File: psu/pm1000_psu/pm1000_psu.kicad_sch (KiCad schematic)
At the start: 48 parts, among them J1 Screw_Terminal_01x04, J10 Conn_01x03_Male, J2 Conn_01x03_Male, J3 Phantom A switch, J4 Phantom A Led, J5 Conn_01x02_Male, J6 Conn_01x03_Male, J7 Phantom B switch, J8 Phantom B Led, J9 Conn_01x03_Male, U1 LM317_TO-220, U2 LM317_TO-220, U3 LM317_TO-220

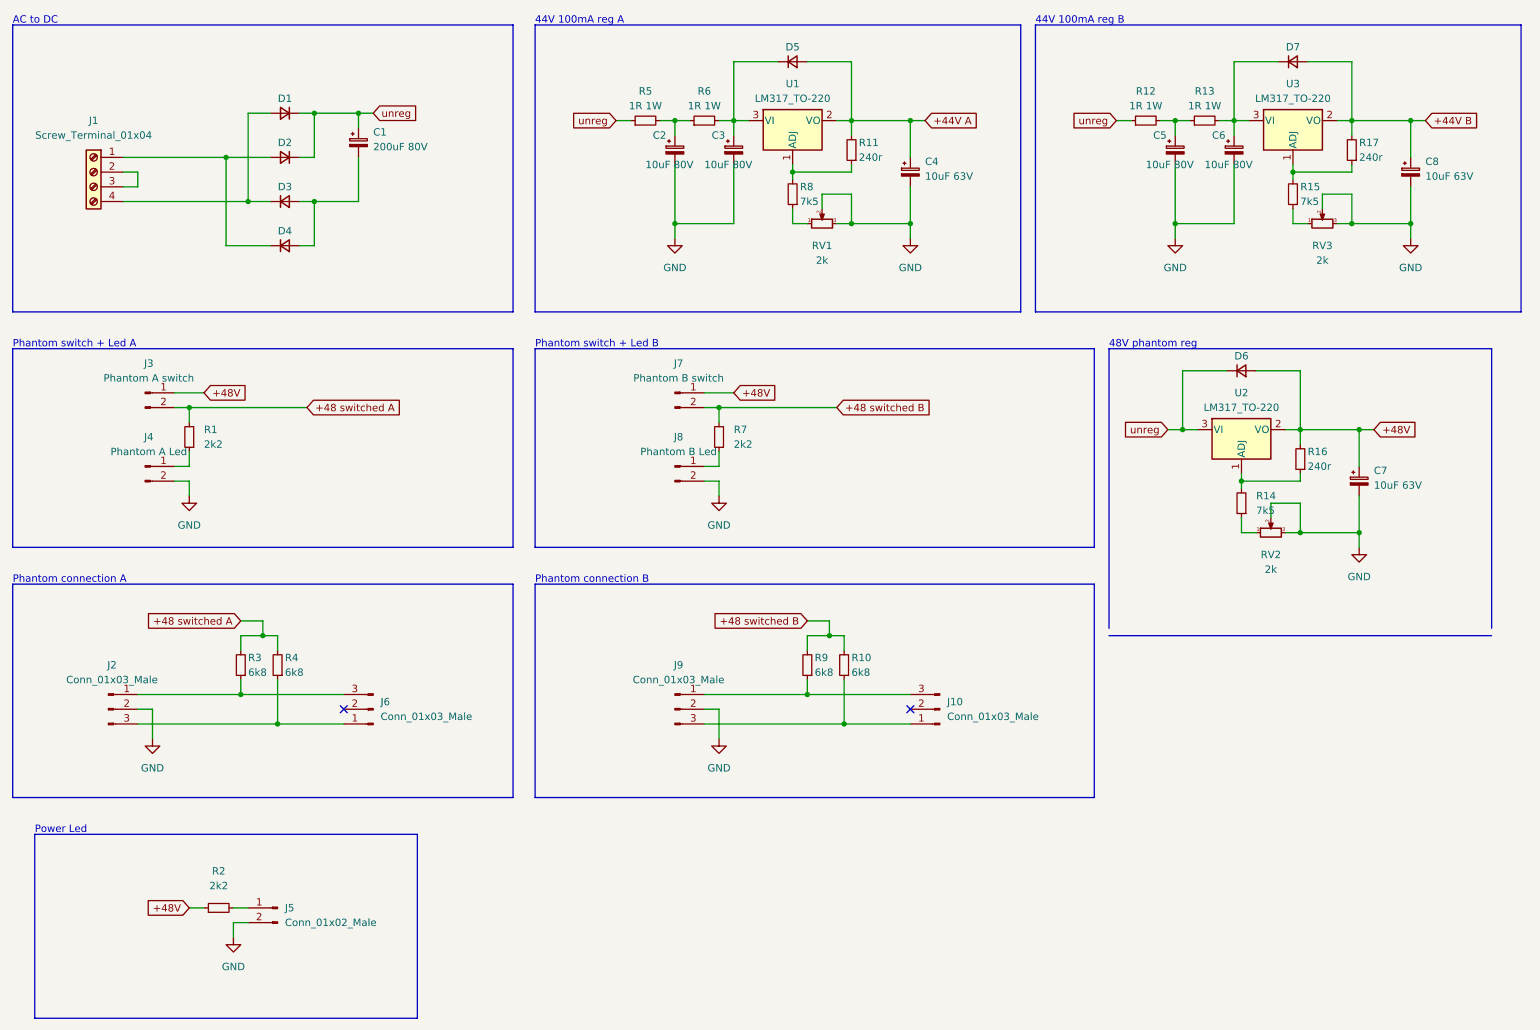
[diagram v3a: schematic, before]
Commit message: add rest of the footprints
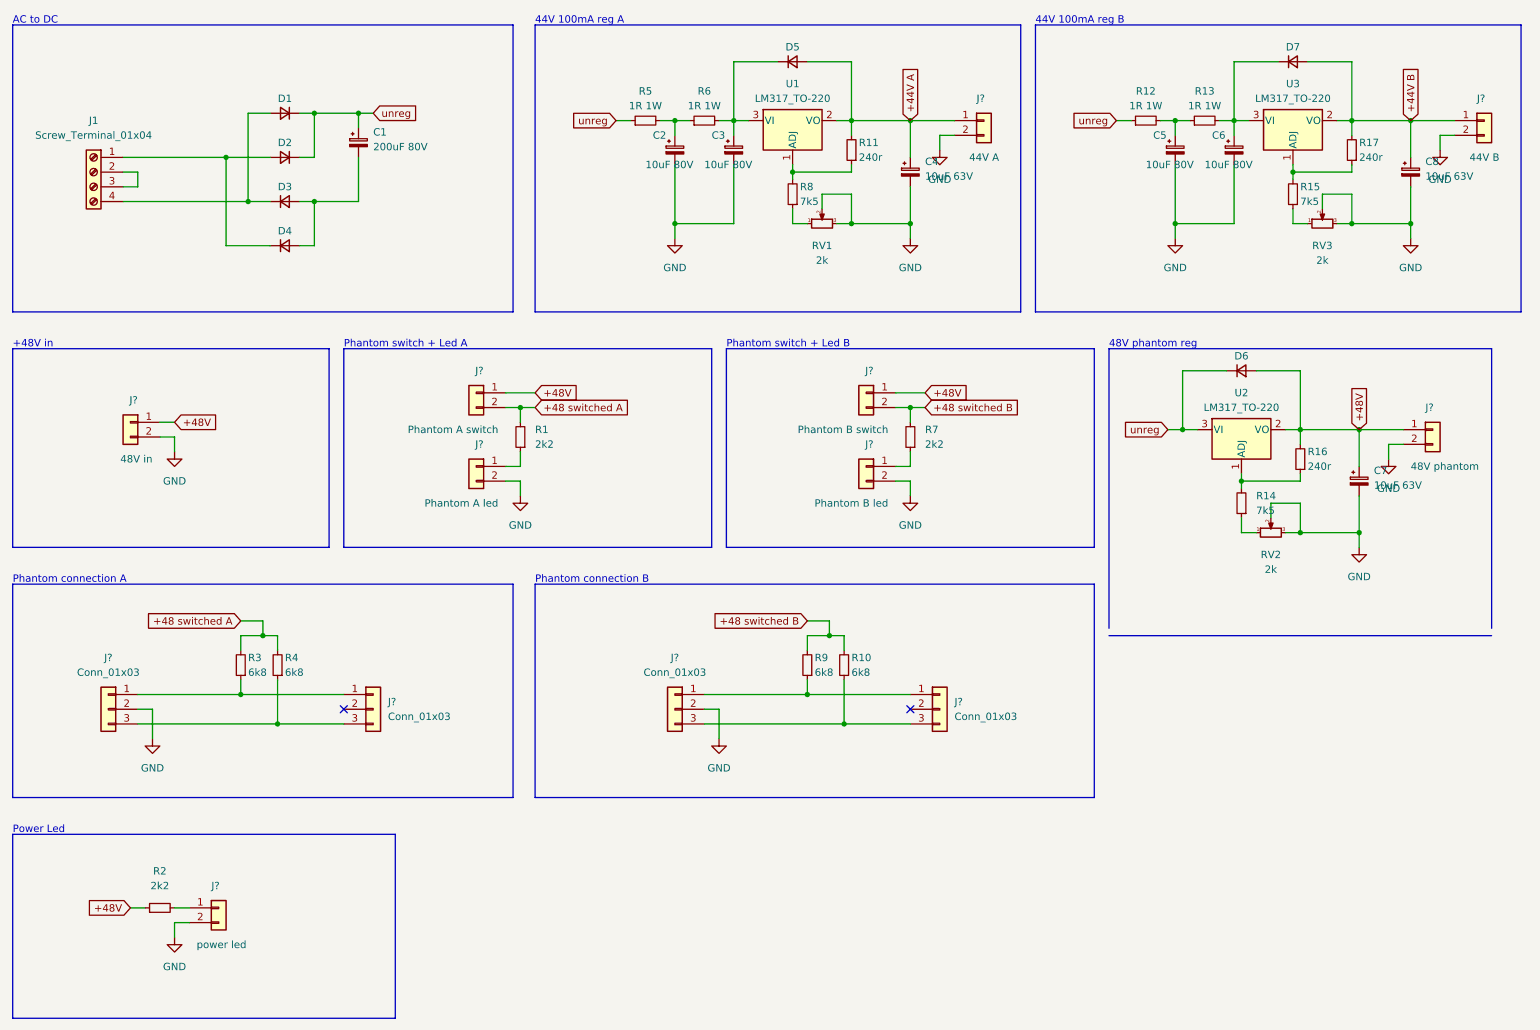
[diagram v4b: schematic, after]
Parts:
- removed J10, J2, J6, J9: Conn_01x03_Male, symbol Connector:Conn_01x03_Male
- removed J3: Phantom A switch, symbol Connector:Conn_01x02_Male
- removed J4: Phantom A Led, symbol Connector:Conn_01x02_Male
- removed J5: Conn_01x02_Male, symbol Connector:Conn_01x02_Male
- removed J7: Phantom B switch, symbol Connector:Conn_01x02_Male
- removed J8: Phantom B Led, symbol Connector:Conn_01x02_Male
- added J? (x4): Conn_01x03, Connector_Molex:Molex_KK-396_A-41791-0003_1x03_P3.96mm_Vertical, symbol Connector_Generic:Conn_01x03
- added J?: Phantom A led, Connector_Molex:Molex_KK-396_A-41791-0002_1x02_P3.96mm_Vertical, symbol Connector_Generic:Conn_01x02
- added J?: power led, Connector_Molex:Molex_KK-396_A-41791-0002_1x02_P3.96mm_Vertical, symbol Connector_Generic:Conn_01x02
- added J?: Phantom A switch, Connector_Molex:Molex_KK-396_A-41791-0002_1x02_P3.96mm_Vertical, symbol Connector_Generic:Conn_01x02
- added J?: 48V in, Connector_Molex:Molex_KK-396_A-41791-0002_1x02_P3.96mm_Vertical, symbol Connector_Generic:Conn_01x02
- added J?: 44V B, Connector_Molex:Molex_KK-396_A-41791-0002_1x02_P3.96mm_Vertical, symbol Connector_Generic:Conn_01x02
- added J?: 48V phantom, Connector_Molex:Molex_KK-396_A-41791-0002_1x02_P3.96mm_Vertical, symbol Connector_Generic:Conn_01x02
- added J?: Phantom B led, Connector_Molex:Molex_KK-396_A-41791-0002_1x02_P3.96mm_Vertical, symbol Connector_Generic:Conn_01x02
- added J?: Phantom B switch, Connector_Molex:Molex_KK-396_A-41791-0002_1x02_P3.96mm_Vertical, symbol Connector_Generic:Conn_01x02
- added J?: 44V A, Connector_Molex:Molex_KK-396_A-41791-0002_1x02_P3.96mm_Vertical, symbol Connector_Generic:Conn_01x02
- J1: footprint (none) -> TerminalBlock_Phoenix:TerminalBlock_Phoenix_PT-1,5-4-5.0-H_1x04_P5.00mm_Horizontal
- RV1, RV2, RV3: footprint Potentiometer_THT:Potentiometer_Bourns_3386F_Vertical -> Potentiometer_THT:Potentiometer_Piher_PT-10-V05_Vertical
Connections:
- net +44V A: now also J?.1 (Pin_1)
- net +44V B: now also J?.1 (Pin_1)
- net +48 switched A: now also J?.2 (Pin_2)
- net +48 switched B: now also J?.2 (Pin_2)
- net +48V: now also J?.1 (Pin_1), J?.1 (Pin_1), J?.1 (Pin_1), J?.1 (Pin_1)
- net GND: now also J?.2 (Pin_2), J?.2 (Pin_2), J?.2 (Pin_2), J?.2 (Pin_2), J?.2 (Pin_2), J?.2 (Pin_2), J?.2 (Pin_2), J?.2 (Pin_2), J?.2 (Pin_2)
- net at R3.1: now also J?.1 (Pin_1), J?.1 (Pin_1)
- net at R4.1: now also J?.3 (Pin_3), J?.3 (Pin_3)
- net at R1.1: now also J?.1 (Pin_1)
- net at R10.1: now also J?.3 (Pin_3), J?.3 (Pin_3)
- net at R2.2: now also J?.1 (Pin_1)
- net at R9.1: now also J?.1 (Pin_1), J?.1 (Pin_1)
- net at R7.1: now also J?.1 (Pin_1)
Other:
- note added: "+48V in"
- moved on the sheet: R1, R2, R7

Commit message: split psu and phantom pcb
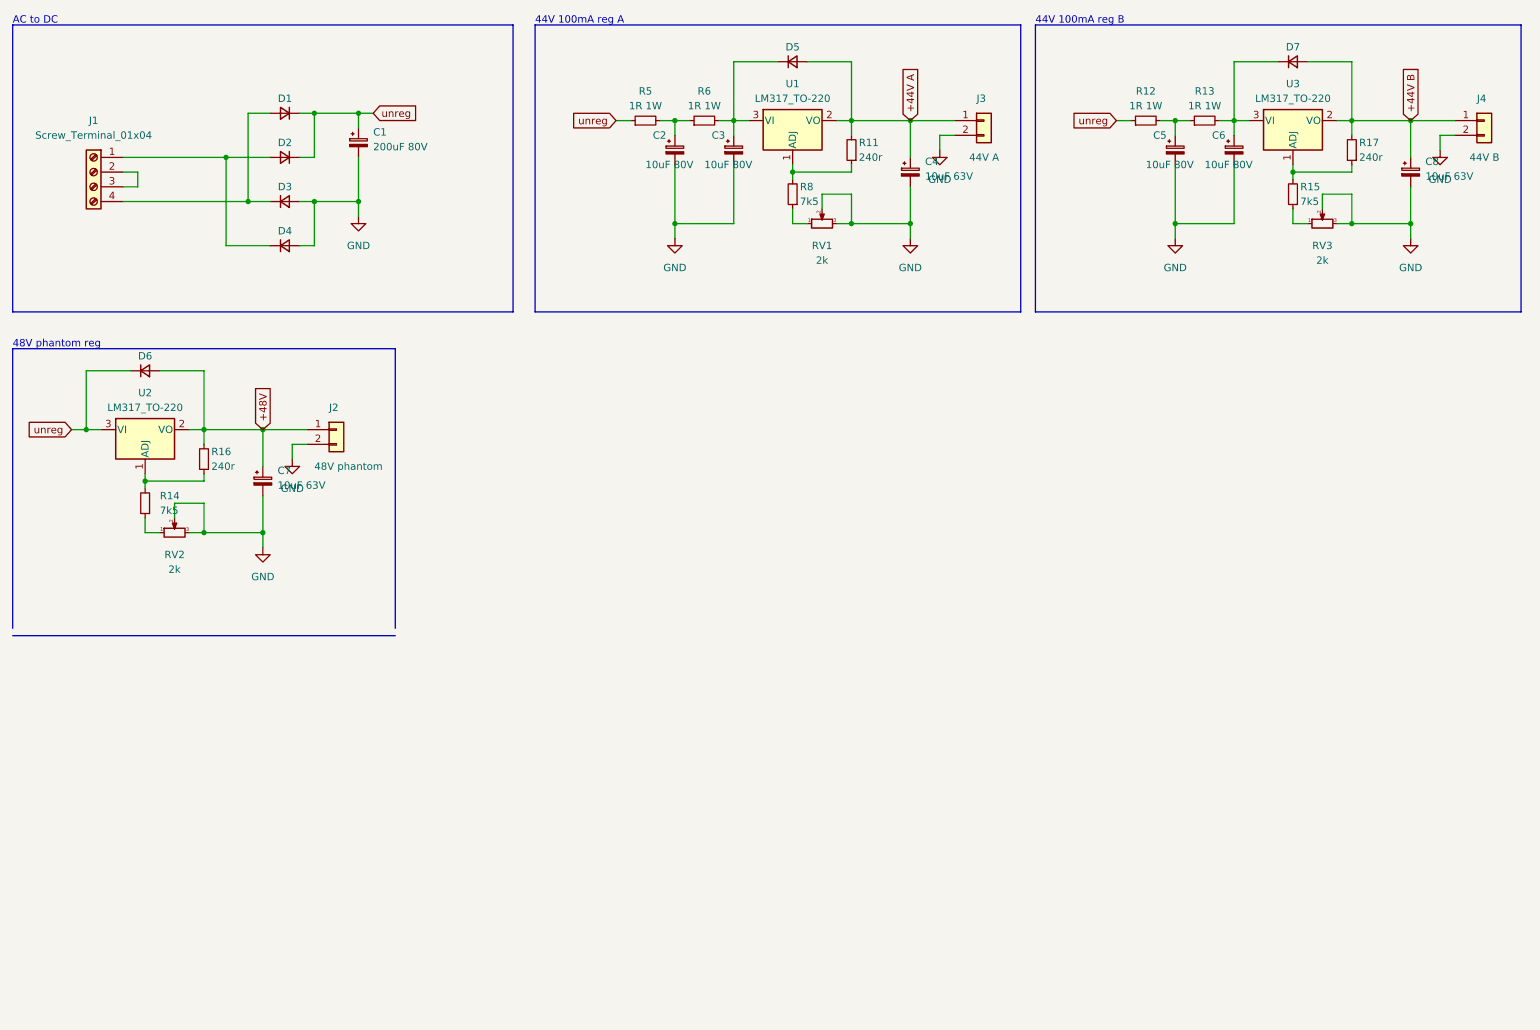
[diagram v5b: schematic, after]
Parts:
- removed J? (x4): Conn_01x03, Connector_Molex:Molex_KK-396_A-41791-0003_1x03_P3.96mm_Vertical, symbol Connector_Generic:Conn_01x03
- removed J?: Phantom A led, Connector_Molex:Molex_KK-396_A-41791-0002_1x02_P3.96mm_Vertical, symbol Connector_Generic:Conn_01x02
- removed J?: power led, Connector_Molex:Molex_KK-396_A-41791-0002_1x02_P3.96mm_Vertical, symbol Connector_Generic:Conn_01x02
- removed J?: Phantom A switch, Connector_Molex:Molex_KK-396_A-41791-0002_1x02_P3.96mm_Vertical, symbol Connector_Generic:Conn_01x02
- removed J?: 48V in, Connector_Molex:Molex_KK-396_A-41791-0002_1x02_P3.96mm_Vertical, symbol Connector_Generic:Conn_01x02
- removed J?: Phantom B led, Connector_Molex:Molex_KK-396_A-41791-0002_1x02_P3.96mm_Vertical, symbol Connector_Generic:Conn_01x02
- removed J?: Phantom B switch, Connector_Molex:Molex_KK-396_A-41791-0002_1x02_P3.96mm_Vertical, symbol Connector_Generic:Conn_01x02
- removed R1, R2, R7: 2k2, Resistor_THT:R_Axial_DIN0207_L6.3mm_D2.5mm_P10.16mm_Horizontal, symbol Device:R_Small
- removed R10, R3, R4, R9: 6k8, Resistor_THT:R_Axial_DIN0207_L6.3mm_D2.5mm_P10.16mm_Horizontal, symbol Device:R_Small
- gave numbers to parts that had none: 3
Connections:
- net GND: now also C1.2, D3.2 (A), D4.2 (A)
- no-connect marks 2 -> 0
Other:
- note removed: "+48V in"
- note removed: "Phantom connection A"
- note removed: "Phantom connection B"
- note removed: "Phantom switch + Led A"
- note removed: "Phantom switch + Led B"
- note removed: "Power Led"
- moved on the sheet: C7, D6, J2, R14, R16, RV2, U2

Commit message: layout and route pcb board
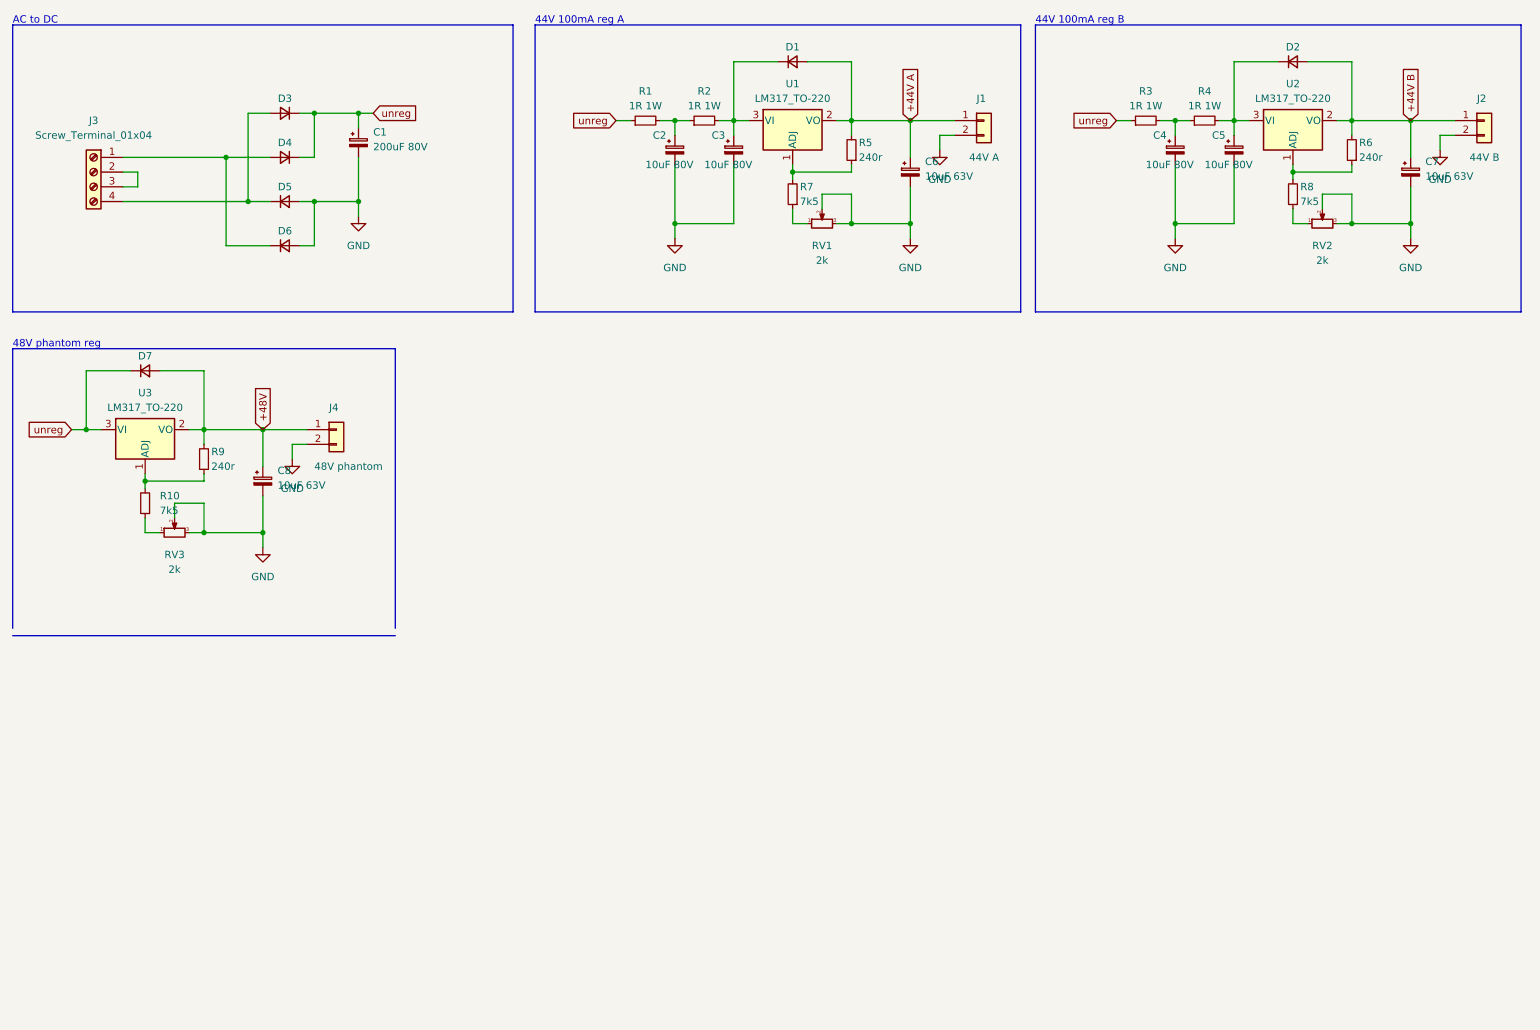
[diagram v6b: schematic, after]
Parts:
- J1: renamed from J3; footprint Connector_Molex:Molex_KK-396_A-41791-0002_1x02_P3.96mm_Vertical -> Connector_Molex:Molex_KK-396_5273-02A_1x02_P3.96mm_Vertical
- J2: renamed from J4; footprint Connector_Molex:Molex_KK-396_A-41791-0002_1x02_P3.96mm_Vertical -> Connector_Molex:Molex_KK-396_5273-02A_1x02_P3.96mm_Vertical
- J4: renamed from J2; footprint Connector_Molex:Molex_KK-396_A-41791-0002_1x02_P3.96mm_Vertical -> Connector_Molex:Molex_KK-254_AE-6410-02A_1x02_P2.54mm_Vertical
- renumbered C5 to C4, C6 to C5, C4 to C6, C8 to C7, C7 to C8, D5 to D1, D7 to D2, D1 to D3, D2 to D4, D3 to D5, D4 to D6, D6 to D7, J1 to J3, R5 to R1, R14 to R10, R6 to R2, R12 to R3, R13 to R4, R11 to R5, R17 to R6, R8 to R7, R15 to R8, R16 to R9, RV3 to RV2, RV2 to RV3, U3 to U2, U2 to U3
